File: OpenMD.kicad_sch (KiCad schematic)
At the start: 29 parts, among them J1 GND, J2 Digital, J3 Analog, J4 Sensors, J5 A, J6 B, J7 C, J8 V_{BATT}

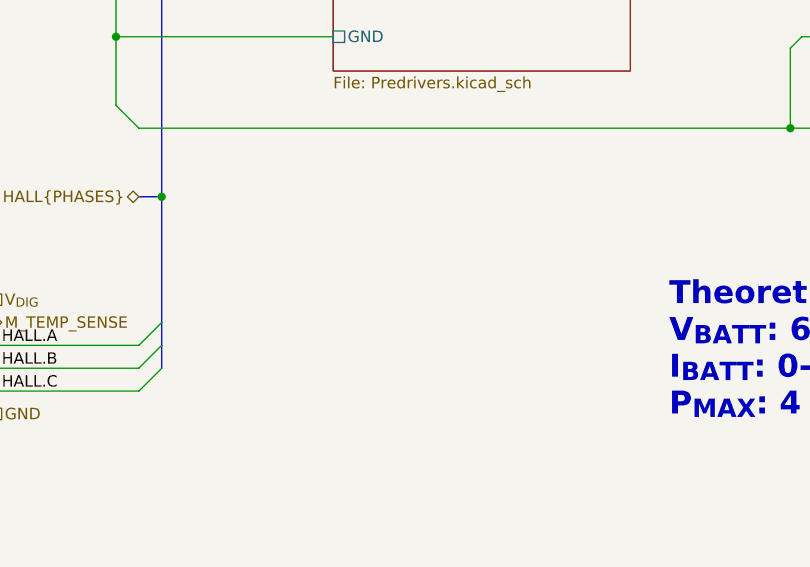
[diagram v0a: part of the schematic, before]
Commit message: added ESD protection
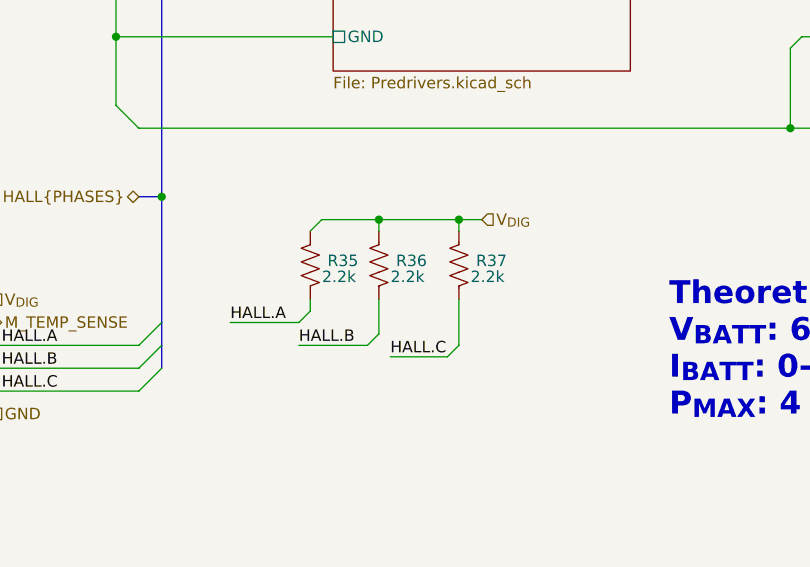
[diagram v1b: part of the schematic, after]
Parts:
- added R35, R36, R37: 2.2k, Resistor_SMD:R_0603_1608Metric, symbol Device:R_US
- R32: Manufacturer_Part_Number SCR0603J10K -> RTT03304JTP
- TH2: value 10k NTC -> 10k NTC
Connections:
- net HALL.A: now also R35.2
- net HALL.B: now also R36.2
- net HALL.C: now also R37.2
- net V_{DIG}: now also R35.1, R36.1, R37.1

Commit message: adjusted according to Reddit feedback
Still needs TVS adjusted
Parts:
- added H5, H7: M2, MountingHole:MountingHole_2.2mm_M2, symbol Mechanical:MountingHole
- D11: value 3.3V -> 3.6V
- J4: symbol Connector_Generic_MountingPin:Conn_01x06_MountingPin -> Connector_Generic:Conn_01x06
- R35, R36, R37: Manufacturer_Part_Number SCR0603J10K -> SCR0603J2K2
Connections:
- net GND: no longer J4.MP (MountPin)
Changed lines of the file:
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@@
 	(wire
 		(pts
-			(xy 95.25 153.67) (xy 92.71 153.67)
-		)
-		(stroke
-			(width 0)
-			(type default)
-		)
-	)
-	(wire
-		(pts
 			(xy 114.3 133.35) (xy 114.3 140.97)
 		)
@@
 	(wire
 		(pts
-			(xy 95.25 153.67) (xy 95.25 157.48)
-		)
-		(stroke
-			(width 0)
-			(type default)
-		)
-	)
-	(wire
-		(pts
 			(xy 114.3 140.97) (xy 116.84 143.51)
 		)
@@
 		)
 	)
-	(hierarchical_label "GND"
-		(shape passive)
-		(at 92.71 153.67 180)
-		(fields_autoplaced yes)
-		(effects
-			(font
-				(size 1.27 1.27)
-			)
-			(justify right)
-		)
-	)
 	(hierarchical_label "V_{ANA}"
 		(shape input)
@@
 			)
 		)
-		(property "Value" "3.3V"
+		(property "Value" "3.6V"
 			(at 104.902 82.042 90)
 			(effects
@@
 	)
 	(symbol
-		(lib_id "Connector_Generic_MountingPin:Conn_01x06_MountingPin")
+		(lib_id "Connector_Generic:Conn_01x06")
 		(at 95.25 170.18 180)
 		(unit 1)
@@
 			)
 		)
-		(property "Description" "Generic connectable mounting pin connector, single row, 01x06, script generated (kicad-library-utils/schlib/autogen/connector/)"
+		(property "Description" "Generic connector, single row, 01x06, script generated (kicad-library-utils/schlib/autogen/connector/)"
 			(at 95.25 170.18 0)
 			(effects
@@
 		(pin "1"
 		)
-		(pin "MP"
-		)
 		(pin "4"
 		)
@@
 	(symbol
 		(lib_id "Mechanical:MountingHole")
+		(at 129.54 189.23 0)
+		(unit 1)
+		(exclude_from_sim yes)
+		(in_bom no)
+		(on_board yes)
+		(dnp no)
+		(fields_autoplaced yes)
+		(property "Reference" "H5"
+			(at 132.08 187.9599 0)
+			(effects
+				(font
+					(size 1.27 1.27)
+				)
+				(justify left)
+			)
+		)
+		(property "Value" "M2"
+			(at 132.08 190.4999 0)
+			(effects
+				(font
+					(size 1.27 1.27)
+				)
+				(justify left)
+			)
+		)
+		(property "Footprint" "MountingHole:MountingHole_2.2mm_M2"
+			(at 129.54 189.23 0)
+			(effects
+				(font
+					(size 1.27 1.27)
+				)
+				(hide yes)
+			)
+		)
+		(property "Datasheet" "~"
+			(at 129.54 189.23 0)
+			(effects
+				(font
+					(size 1.27 1.27)
+				)
+				(hide yes)
+			)
+		)
+		(property "Description" "Mounting Hole without connection"
+			(at 129.54 189.23 0)
+			(effects
+				(font
+					(size 1.27 1.27)
+				)
+				(hide yes)
+			)
+		)
+		(property "Source" "N/A"
+			(at 129.54 189.23 0)
+			(effects
+				(font
+					(size 1.27 1.27)
+				)
+				(hide yes)
+			)
+		)
+		(property "Manufacturer_Part_Number" "N/A"
+			(at 129.54 189.23 0)
+			(effects
+				(font
+					(size 1.27 1.27)
+				)
+				(hide yes)
+			)
+		)
+		(instances
+			(project "OpenMD"
+				(path "/28611c8e-7644-4a1a-8c07-dc86cafc8f6c"
+					(reference "H5")
+					(unit 1)
+				)
+			)
+		)
+	)
+	(symbol
+		(lib_id "Mechanical:MountingHole")
 		(at 307.34 68.58 0)
 		(unit 1)
@@
 			)
 		)
-		(property "Manufacturer_Part_Number" "SCR0603J10K"
+		(property "Manufacturer_Part_Number" "SCR0603J2K2"
 			(at 135.89 158.75 0)
 			(effects
@@
 			)
 		)
-		(property "Manufacturer_Part_Number" "SCR0603J10K"
+		(property "Manufacturer_Part_Number" "SCR0603J2K2"
 			(at 143.51 158.75 0)
 			(effects
@@
 	)
 	(symbol
+		(lib_id "Mechanical:MountingHole")
+		(at 309.88 196.85 0)
+		(unit 1)
+		(exclude_from_sim yes)
+		(in_bom no)
+		(on_board yes)
+		(dnp no)
+		(fields_autoplaced yes)
+		(property "Reference" "H7"
+			(at 312.42 195.5799 0)
+			(effects
+				(font
+					(size 1.27 1.27)
+				)
+				(justify left)
+			)
+		)
+		(property "Value" "M2"
+			(at 312.42 198.1199 0)
+			(effects
+				(font
+					(size 1.27 1.27)
+				)
+				(justify left)
+			)
+		)
+		(property "Footprint" "MountingHole:MountingHole_2.2mm_M2"
+			(at 309.88 196.85 0)
+			(effects
+				(font
+					(size 1.27 1.27)
+				)
+				(hide yes)
+			)
+		)
+		(property "Datasheet" "~"
+			(at 309.88 196.85 0)
+			(effects
+				(font
+					(size 1.27 1.27)
+				)
+				(hide yes)
+			)
+		)
+		(property "Description" "Mounting Hole without connection"
+			(at 309.88 196.85 0)
+			(effects
+				(font
+					(size 1.27 1.27)
+				)
+				(hide yes)
+			)
+		)
+		(property "Source" "N/A"
+			(at 309.88 196.85 0)
+			(effects
+				(font
+					(size 1.27 1.27)
+				)
+				(hide yes)
+			)
+		)
+		(property "Manufacturer_Part_Number" "N/A"
+			(at 309.88 196.85 0)
+			(effects
+				(font
+					(size 1.27 1.27)
+				)
+				(hide yes)
+			)
+		)
+		(instances
+			(project "OpenMD"
+				(path "/28611c8e-7644-4a1a-8c07-dc86cafc8f6c"
+					(reference "H7")
+					(unit 1)
+				)
+			)
+		)
+	)
+	(symbol
 		(lib_id "Connector_Generic_MountingPin:Conn_01x12_MountingPin")
 		(at 95.25 109.22 0)
@@
 			)
 		)
-		(property "Manufacturer_Part_Number" "SCR0603J10K"
+		(property "Manufacturer_Part_Number" "SCR0603J2K2"
 			(at 152.4 158.75 0)
 			(effects

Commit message: added all changes from Reddit
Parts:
- added D33, D34, D35: 5V, Diode_SMD:D_0603_1608Metric, symbol Device:D_TVS_Small
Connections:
- net GND: now also D33.1 (A1), D34.1 (A1), D35.1 (A1)
- net HALL.A: now also D35.2 (A2)
- net HALL.B: now also D34.2 (A2)
- net HALL.C: now also D33.2 (A2)
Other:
- moved on the sheet: R35

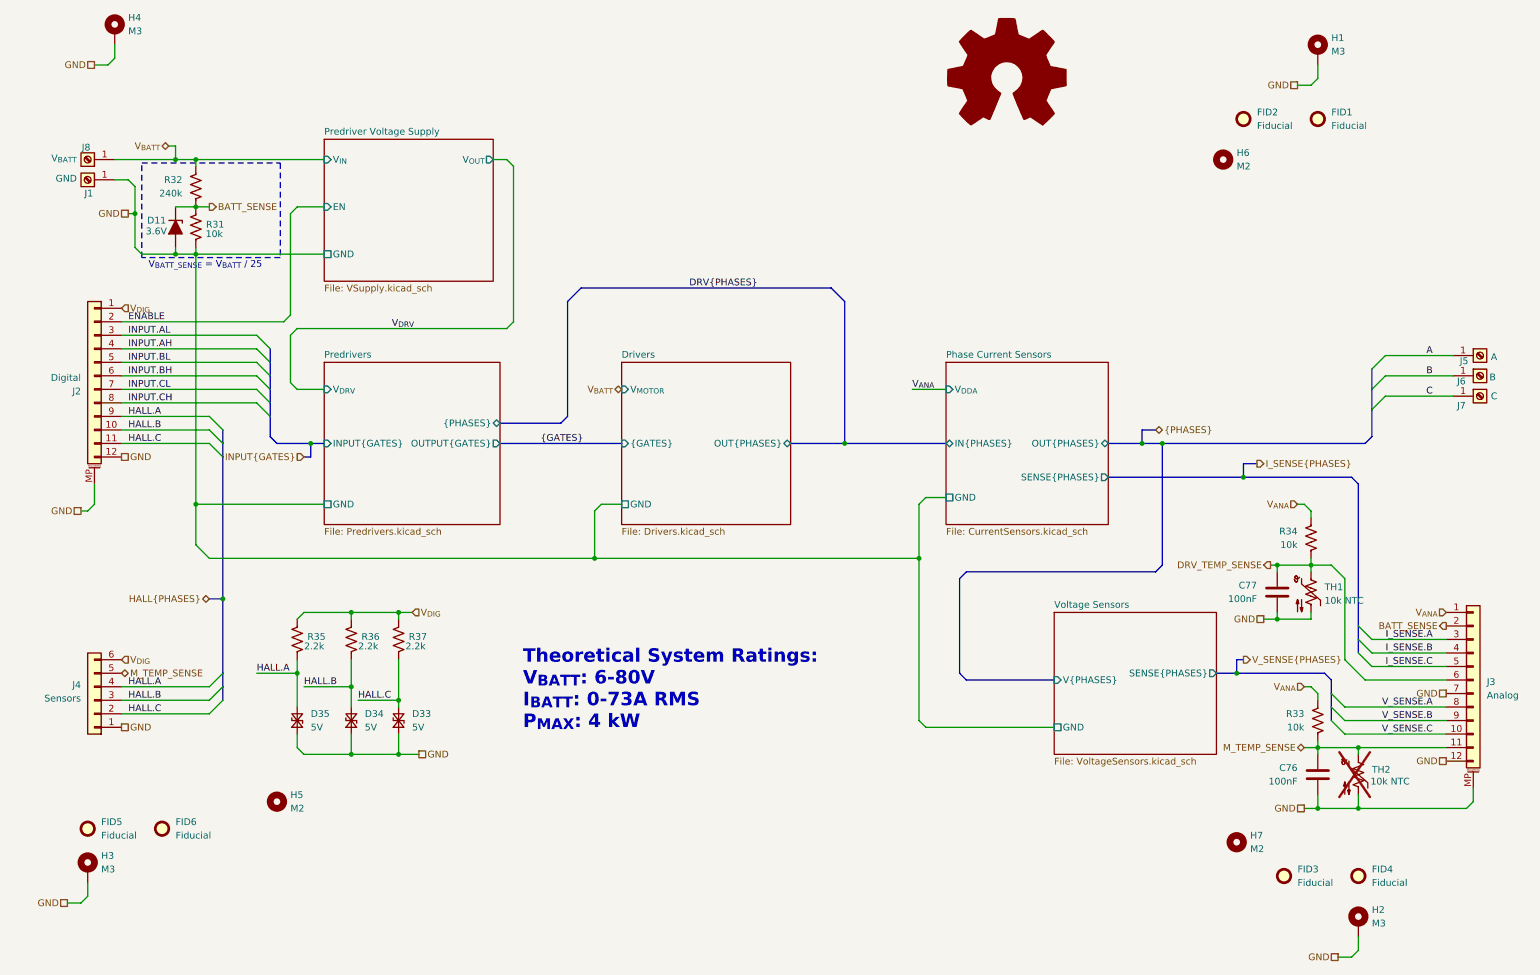
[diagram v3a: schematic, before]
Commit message: Removed Hall Sensors for Scalability
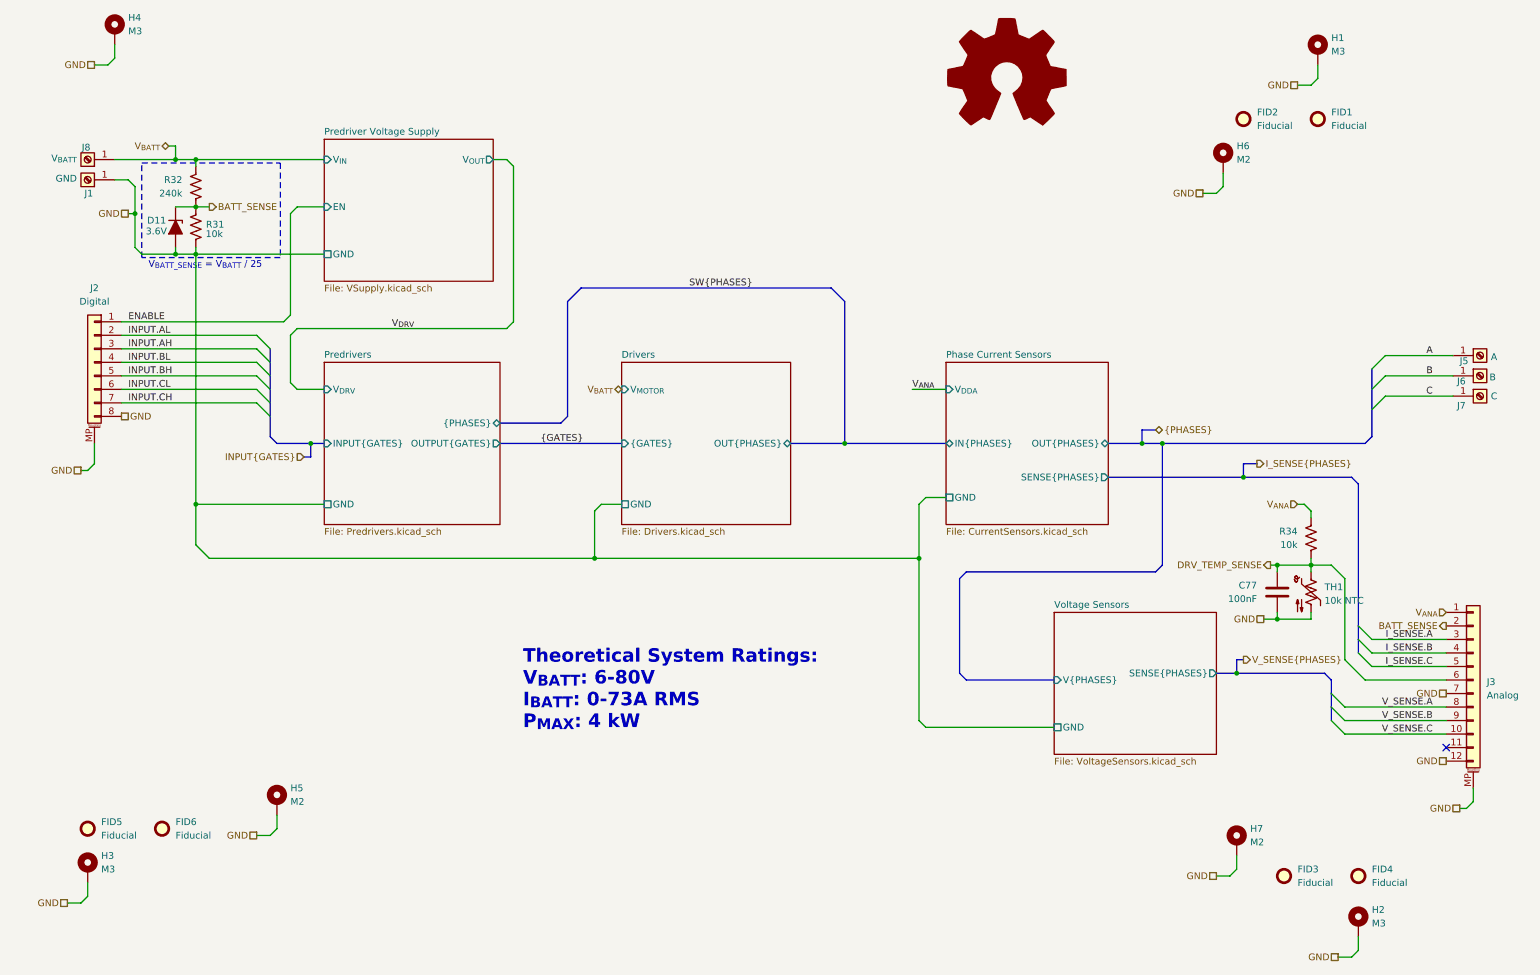
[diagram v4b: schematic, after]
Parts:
- removed C76: 100nF, Capacitor_SMD:C_0603_1608Metric, symbol Device:C
- removed D33, D34, D35: 5V, Diode_SMD:D_0603_1608Metric, symbol Device:D_TVS_Small
- removed J2: Digital, Connector_JST:JST_SH_SM12B-SRSS-TB_1x12-1MP_P1.00mm_Horizontal, symbol Connector_Generic_MountingPin:Conn_01x12_MountingPin
- removed J4: Sensors, Connector_JST:JST_PH_S6B-PH-K_1x06_P2.00mm_Horizontal, symbol Connector_Generic:Conn_01x06
- removed R33: 10k, Resistor_SMD:R_0603_1608Metric, symbol Device:R_US
- removed R35, R36, R37: 2.2k, Resistor_SMD:R_0603_1608Metric, symbol Device:R_US
- removed TH2: 10k NTC, Resistor_SMD:R_0603_1608Metric, symbol Device:Thermistor_NTC_US
- added J2: Digital, Connector_JST:JST_SH_SM08B-SRSS-TB_1x08-1MP_P1.00mm_Horizontal, symbol Connector_Generic_MountingPin:Conn_01x08_MountingPin
- H5: footprint MountingHole:MountingHole_2.2mm_M2 -> MountingHole:MountingHole_2.2mm_M2_ISO7380_Pad_TopOnly; symbol Mechanical:MountingHole -> Mechanical:MountingHole_Pad
- H6, H7: footprint MountingHole:MountingHole_2.2mm_M2 -> MountingHole:MountingHole_2.2mm_M2_DIN965_Pad_TopOnly; symbol Mechanical:MountingHole -> Mechanical:MountingHole_Pad
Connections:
- net ENABLE: now also J2.1 (Pin_1)
- net GND: now also H5.1, H6.1, H7.1, J2.8 (Pin_8), J2.MP (MountPin)
- net INPUT.AH: now also J2.3 (Pin_3)
- net INPUT.AL: now also J2.2 (Pin_2)
- net INPUT.BH: now also J2.5 (Pin_5)
- net INPUT.BL: now also J2.4 (Pin_4)
- net INPUT.CH: now also J2.7 (Pin_7)
- net INPUT.CL: now also J2.6 (Pin_6)
- net M_TEMP_SENSE: no longer names the net of J3.11 (Pin_11)
- no-connect marks 0 -> 1

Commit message: updates to make better
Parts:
- D11: value 3.6V -> 3.3V
- J2: Manufacturer_Part_Number (none) -> SM08B-SRSS-TB(LF)(SN); Source (none) -> LCSC
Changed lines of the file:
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@@
 			)
 		)
-		(property "Value" "3.6V"
+		(property "Value" "3.3V"
 			(at 104.902 82.042 90)
 			(effects
@@
 			(at 95.25 106.68 0)
 			(effects
+				(font
+					(size 1.27 1.27)
+				)
+				(hide yes)
+			)
+		)
+		(property "Manufacturer_Part_Number" "SM08B-SRSS-TB(LF)(SN)"
+			(at 95.25 106.68 0)
+			(effects
+				(font
+					(size 1.27 1.27)
+				)
+				(hide yes)
+			)
+		)
+		(property "Source" "LCSC"
+			(at 95.25 106.68 0)
+			(effects

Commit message: revision 2
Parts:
- removed D11: 3.3V, Diode_SMD:D_SOD-323, symbol Device:D_Zener_Filled
- added C63: 100nF, Capacitor_SMD:C_0402_1005Metric, symbol Device:C
- C77: footprint Capacitor_SMD:C_0603_1608Metric -> Capacitor_SMD:C_0402_1005Metric; Manufacturer_Part_Number CGA0603X7R104K101JT -> (none); Rating 100V -> 5V
- R31, R32, R34, TH1: footprint Resistor_SMD:R_0603_1608Metric -> Resistor_SMD:R_0402_1005Metric
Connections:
- net BATT_SENSE: now also C63.1
- net GND: now also C63.2
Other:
- moved on the sheet: R31, R32
